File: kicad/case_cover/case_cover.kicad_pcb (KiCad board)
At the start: 2 copper layers, 73 x 90.5 mm, 3 parts, among them J2 Conn_01x04

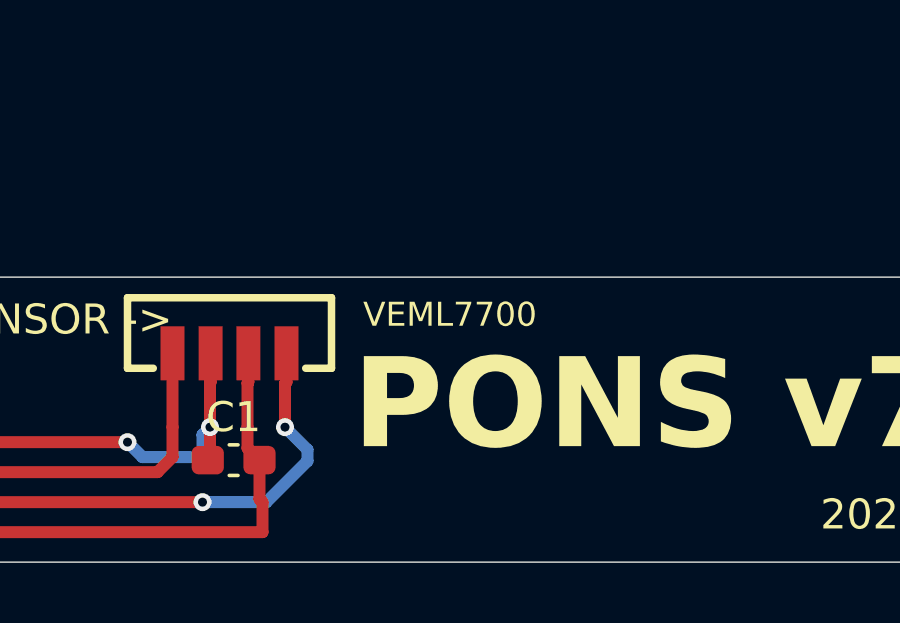
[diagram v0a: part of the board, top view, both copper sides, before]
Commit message: 0.994 GNSS の翌日起動を速くし、本番前チェック・高温充電の警告・電池低下の点滅を入れ、v7.1 基板の逆接保護と発注前の修正を仕上げた
- GNSS: AssistNow Autonomous を有効化（CFG-VALSET で RAM と BBR。settings.h の
  GNSS_USE_ANA。0 でも OFF を書き込む＝BBR に残った ON を消すため）。前日と同じ時間帯の
  起動が 23〜28 秒 → 3〜4 秒（BT1 が生きていること）。NAV-AOPSTATUS を 1Hz で受け、
  GNSS DETAIL 3 に ANA:ON data/use/calc、log.txt に「... after boot」（TTFF）・最初の
  測位の軌道の出どころ・10 分ごとの計算時間。ACK 待ちの間も imu_service_if_due() を
  呼ぶ（以前からの抜け）
- readiness.cpp（新規）: 本番前チェック。GNSS・IMU・ESKF・較正（マウント外れだけ。
  日付またぎは推測なので入れない＝台の上での APPLY を促さない）・地上の姿勢・設定画面の
  赤丸・USB・電池 50%・SD・無線（送信モード）がそろい、地上で止まっていたら 1 度だけ
  「準備完了」（ready.wav）。欠けていれば設定画面の右上に項目名。受信モード・リプレイ・
  デモは対象外。既存の判定を読むだけで、条件は書き写さない
- 高温での充電の警告（v7・v7.1）: USB 接続中に MS5611 が 45°C を 30 秒超え続けたら
  地図に TOO HOT TO CHARGE と charge_hot.wav（60 秒ごと・最低音量 60）。電池の仕様は
  充電 0〜45°C。地図の段は電源異常と共用（異常 ＞ 高温 ＞ SW OFF）
- 電池低下のときの点滅（v7.1）: 電池低下の警告と同じ 3.5V でバックライトを 2 秒点灯・
  4 秒消灯。3.65V か USB で戻る（3.5V で戻すと入り切りをくり返す）。消灯中も本来の
  明るさは追い続ける（照度追従の立ち上がりで 2 秒の点灯が暗くならないように）
- 本体の回路図・PCB: 電池の逆接保護 Q4（AO3401A、D が電池側）＋ R52、PWR1 の
  ネットを VBAT_RAW に。C32 を 10µF 0805 に（10/20 に直したのが 0402 に戻っていた）。
  D5 を RB751S40（逆流が少ない。PCBA で実装）に。古いメモを整理
- IMU 基板の GND が IC1.16・C3 だけ分かれていたのをつないだ。J3 の値を 01x08 に。
  case_cover の部品番号を回路図と一致。GNSS 基板の裏面を GND ベタに（浮いていた
  19 個のビアがつながった）
- 音声 2 本（ready / charge_hot）は macOS の音声合成の仮音声
- docs: pons_power.md に Q4・P-ch FET 3 段の役割・電池の保護回路（DTP603048(PHR) の
  仕様書）・R39 を 2.2kΩ に戻さない理由（電池の最大充電 430mA も超える）・高温の警告・
  電池低下の点滅。README に GNSS の起動・本番前チェック・新しい警報・v7.1 の USB-C と
  充電時間、古い記述（v7 の実結線試験・無線の立ち上げ手順書の冒頭）を今の状態に。
  CLAUDE.md に BBR に書いた GNSS 設定が残る件と readiness.cpp
- kicad/.gitignore に *.pos

PONS_BOARD は V7 と V71 の両方でビルド OK（4,052,376 / 4,046,728 B）/
gen_wav_flash.py --check は 37 ファイル一致 / 本体 PCB の DRC は未配線 0・回路図と一致
（シルクの 6 件は意図どおり）/ IMU・カバー・GNSS 基板も未配線 0・回路図と一致 /
BOM の LCSC 番号は全 48 種類を JLC/LCSC の部品情報と照合 / 実機は未確認

Co-Authored-By: Claude Opus 5.5 <noreply@anthropic.com>
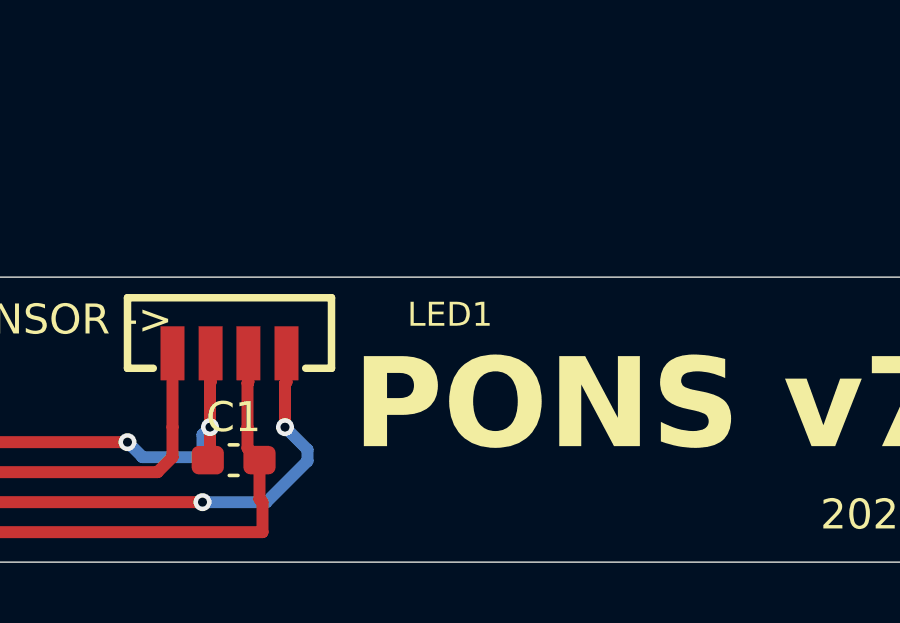
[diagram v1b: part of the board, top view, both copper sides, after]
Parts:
- renumbered VEML7700 to LED1
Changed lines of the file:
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@@
 		(layer "F.Cu")
 		(at 127.4 148.5375)
-		(property "Reference" "VEML7700"
+		(property "Reference" "LED1"
 			(at 7.35 -1.2875 0)
 			(layer "F.SilkS")
